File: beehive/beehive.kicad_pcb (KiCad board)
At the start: 2 copper layers, 23 parts, among them J1 M05PTH, Q1 MMBT4403, U1 ESP32-S3-WROOM-1U, U2 HX711, U3 ADXL362

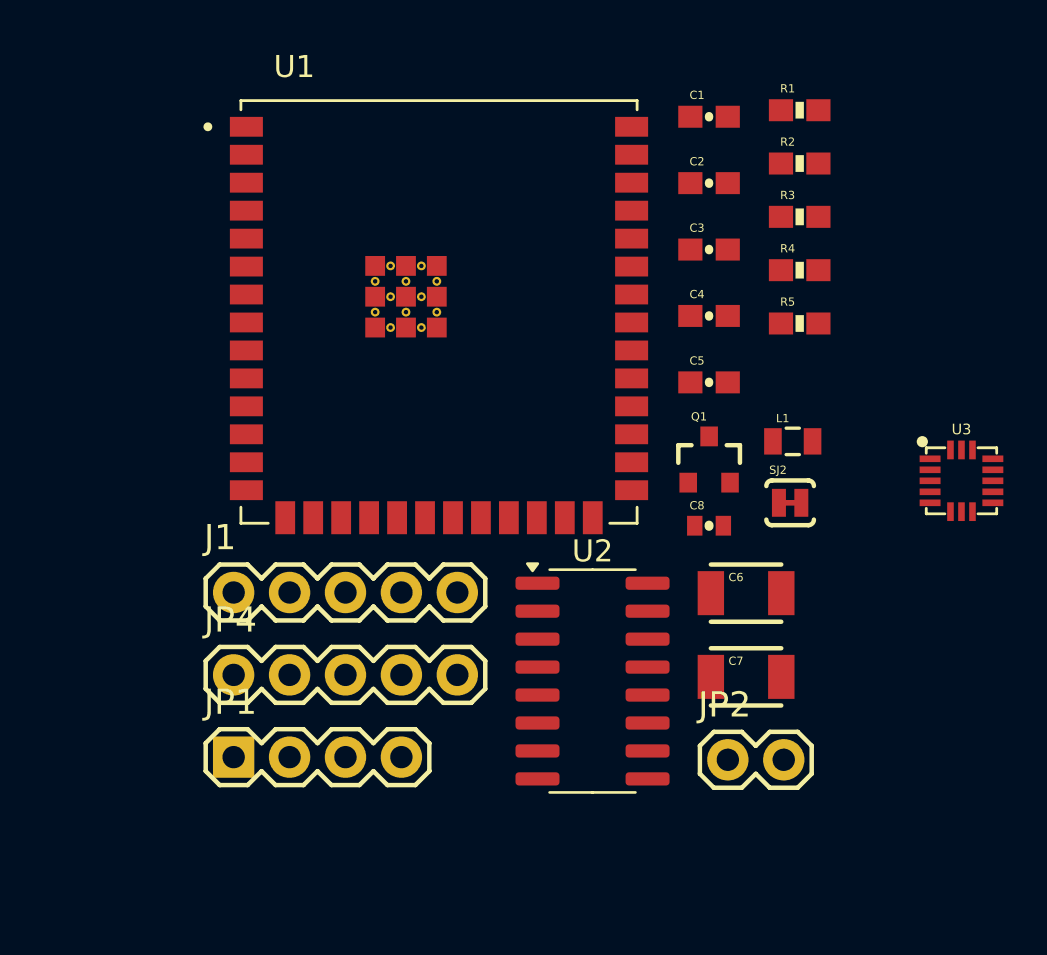
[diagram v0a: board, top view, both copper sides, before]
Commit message: added custom library submodule
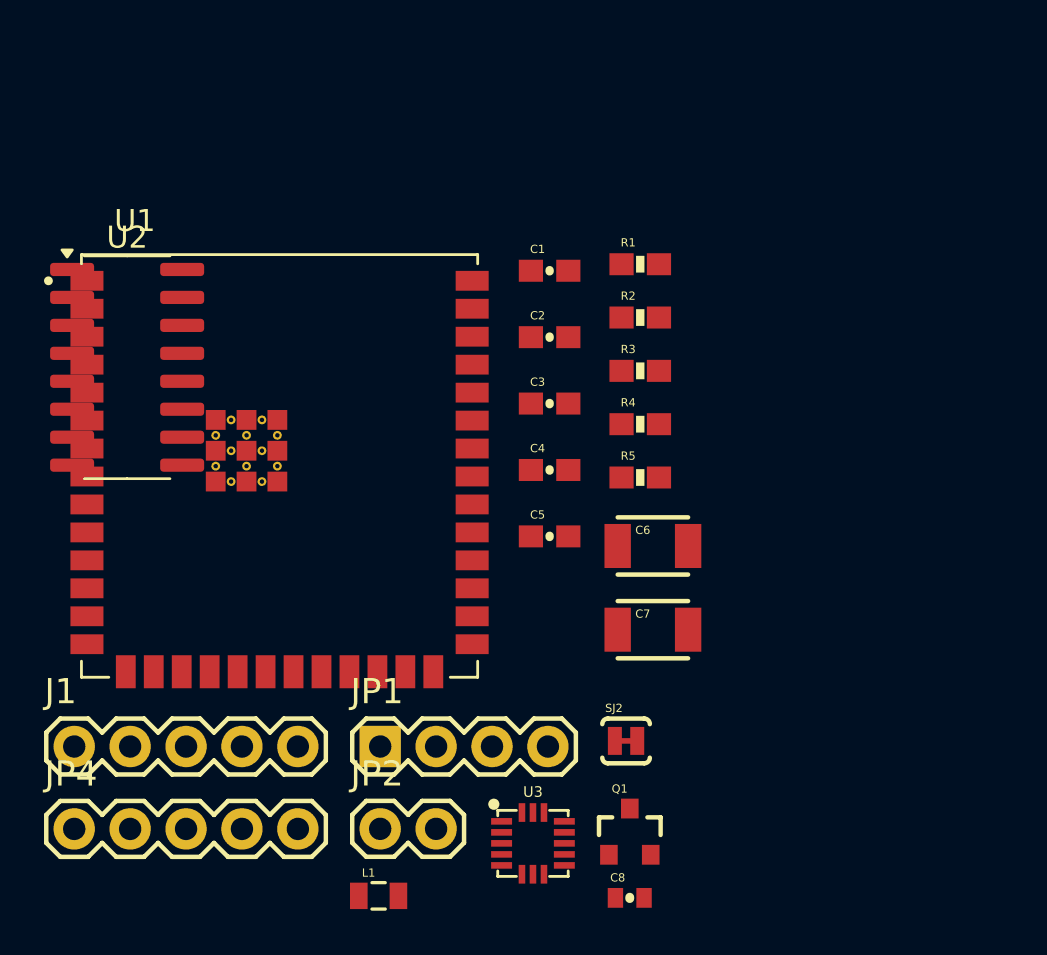
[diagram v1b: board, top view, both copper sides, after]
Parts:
- C1, C2, C3, C4, C5: footprint SparkFun_HX711_Load_Cell:0603-CAP -> Board_SparkFun_HX711_Load_Cell:0603-CAP
- C6, C7: footprint SparkFun_HX711_Load_Cell:1210 -> Board_SparkFun_HX711_Load_Cell:1210
- C8: footprint ADXL362 BOB v01:0402-CAP -> Board_ADXL362_BOB_v01:0402-CAP
- J1, JP4: footprint SparkFun_HX711_Load_Cell:1X05 -> Board_SparkFun_HX711_Load_Cell:1X05
- JP1: footprint ADXL362 BOB v01:1X04 -> Board_ADXL362_BOB_v01:1X04
- JP2: footprint SparkFun_HX711_Load_Cell:1X02 -> Board_SparkFun_HX711_Load_Cell:1X02
- L1: footprint SparkFun_HX711_Load_Cell:0805 -> Board_SparkFun_HX711_Load_Cell:0805
- Q1: footprint SparkFun_HX711_Load_Cell:SOT23-3 -> Board_SparkFun_HX711_Load_Cell:SOT23-3
- R1, R2, R3, R4, R5: footprint SparkFun_HX711_Load_Cell:0603-RES -> Board_SparkFun_HX711_Load_Cell:0603-RES
- SJ2: footprint SparkFun_HX711_Load_Cell:PAD-JUMPER-2-NC_BY_TRACE_YES_SILK -> Board_SparkFun_HX711_Load_Cell:PAD-JUMPER-2-NC_BY_TRACE_YES_SILK
- U1: footprint ESP32:XCVR_ESP32-S3-WROOM-1U -> ESP32-S3-WROOM-1:XCVR_ESP32-S3-WROOM-1U
- U3: footprint adxl362:LGA-16-3X2.5 -> ADXL362:LGA-16-3X2.5
- moved L1 27.9 mm to (103.6, 78.7)
- moved U3 25.5 mm to (110.6, 76.3)
- moved U2 25.5 mm to (92.2, 54.7)
- moved C8 17.3 mm to (115.0, 78.8)
- moved Q1 17.3 mm to (115.0, 75.8)
- moved JP2 16.1 mm to (103.7, 75.6)
- moved SJ2 13.1 mm to (114.8, 71.6)
- moved C1 10.1 mm to (111.4, 50.3)
- moved C3 10.1 mm to (111.4, 56.3)
- moved C5 10.1 mm to (111.4, 62.4)
- moved J1 10.1 mm to (89.8, 71.9)
- moved JP4 10.1 mm to (89.8, 75.6)
- moved R2 10.1 mm to (115.5, 52.4)
- moved R3 10.1 mm to (115.5, 54.8)
- moved R4 10.1 mm to (115.5, 57.3)
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
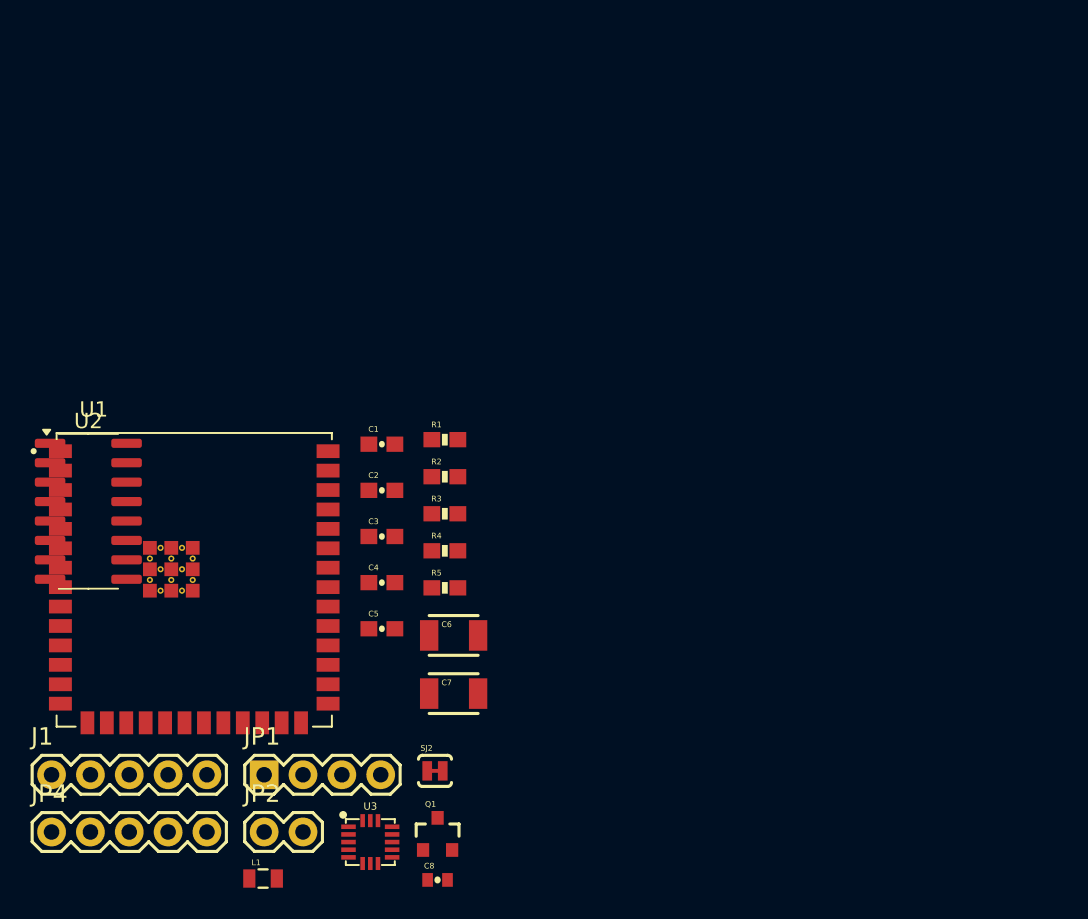
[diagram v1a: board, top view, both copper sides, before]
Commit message: TP5100 and ESP32 remaining
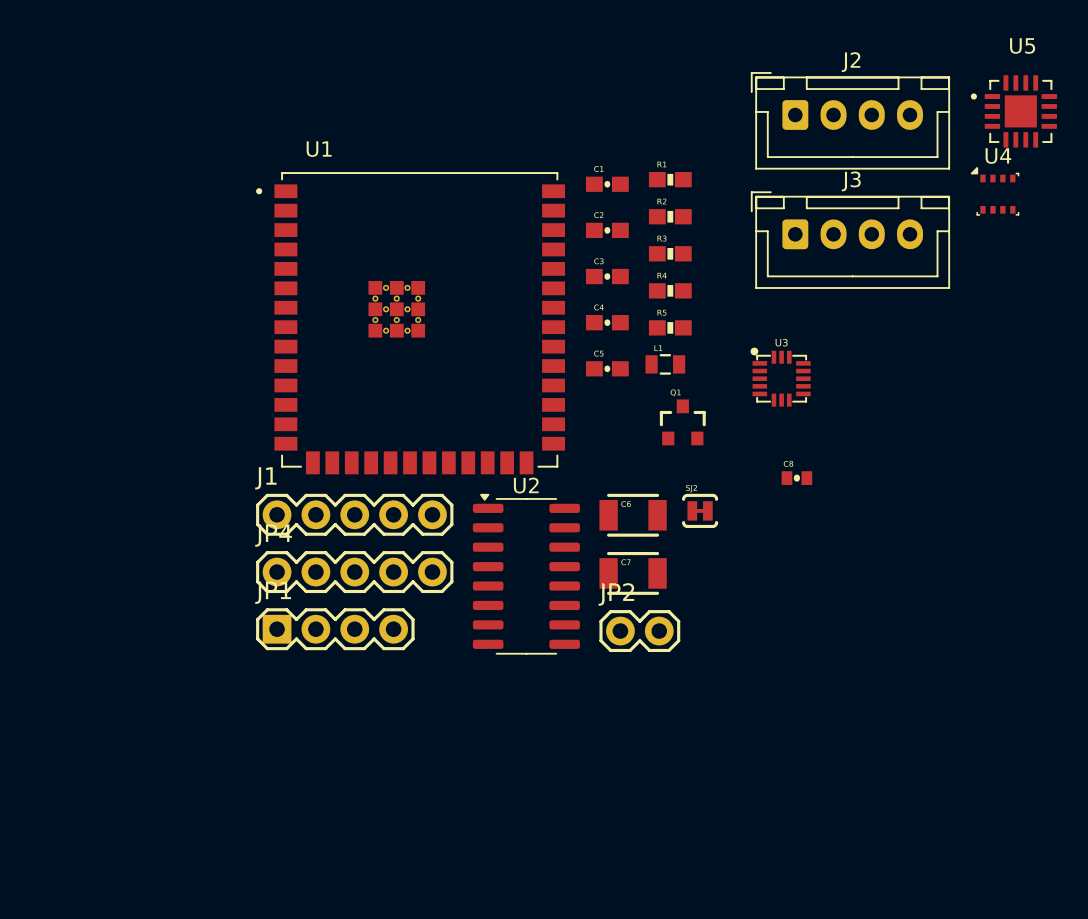
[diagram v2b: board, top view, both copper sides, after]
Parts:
- added J2: Conn_01x04_Pin, Connector_JST:JST_XH_B4B-XH-A_1x04_P2.50mm_Vertical, F.Cu at (138.4, 28.8)
- added J3: Conn_01x04_Pin, Connector_JST:JST_XH_B4B-XH-A_1x04_P2.50mm_Vertical, F.Cu at (138.4, 36.6)
- added U4: BME280, Package_LGA:Bosch_LGA-8_2.5x2.5mm_P0.65mm_ClockwisePinNumbering, F.Cu at (151.6, 33.9)
- added U5: TP5100, TP5100:QFN65P400X400X90-17N, F.Cu at (153.1, 28.5)
- moved L1 42.7 mm to (129.9, 45.1)
- moved U3 40.5 mm to (137.5, 46.0)
- moved C8 35.2 mm to (138.5, 52.5)
- moved Q1 31.3 mm to (131.0, 48.9)
- moved U2 29.0 mm to (120.8, 58.9)
- moved JP2 26.7 mm to (127.0, 62.5)
- moved SJ2 24.3 mm to (132.2, 54.6)
- moved J1 22.5 mm to (104.5, 54.9)
- moved C1 22.5 mm to (126.1, 33.3)
- moved C3 22.5 mm to (126.1, 39.3)
- moved C5 22.5 mm to (126.1, 45.4)
- moved C2 22.5 mm to (126.1, 36.3)
- moved C4 22.5 mm to (126.1, 42.3)
- moved JP4 22.5 mm to (104.5, 58.6)
- moved R2 22.5 mm to (130.2, 35.4)
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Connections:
- C4 pad 2: GND -> unconnected-(C4-Pad2)
- C5 pad 2: GND -> unconnected-(C5-Pad2)
- C6 pad 2: GND -> unconnected-(C6-Pad2)
- U3 pad P$1: unconnected-(U3-VDDIO-PadP$1) -> 3.3V
- U3 pad P$11: unconnected-(U3-INT1-PadP$11) -> Net-(J2-Pin_3)
- U3 pad P$12: Net-(U3-GND-PadP$12) -> GND
- U3 pad P$13: Net-(U3-GND-PadP$12) -> GND
- U3 pad P$14: unconnected-(U3-VS-PadP$14) -> 3.3V
- U3 pad P$16: Net-(U3-GND-PadP$12) -> GND
- U3 pad P$4: unconnected-(U3-SCLK-PadP$4) -> Net-(J3-Pin_4)
- U3 pad P$6: unconnected-(U3-MOSI-PadP$6) -> Net-(J3-Pin_3)
- U3 pad P$7: unconnected-(U3-MISO-PadP$7) -> Net-(J3-Pin_2)
- U3 pad P$8: unconnected-(U3-~{CS}-PadP$8) -> Net-(J3-Pin_1)
- U3 pad P$9: unconnected-(U3-INT2-PadP$9) -> Net-(J2-Pin_4)

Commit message: 123
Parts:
- added C10: 10uF/25V, Capacitor_SMD:C_0603_1608Metric_Pad1.08x0.95mm_HandSolder, F.Cu at (170.3, 85.8)
- added C9: 10uF/25V, Capacitor_SMD:C_0603_1608Metric_Pad1.08x0.95mm_HandSolder, F.Cu at (170.3, 83.3)
- added IC1: MP2307, MP2307:SO8-TH, F.Cu at (165.1, 86.3)
- added U6: MCP1700x-330xxTT, Package_TO_SOT_SMD:SOT-23, F.Cu at (170.6, 89.5)
- C8: value .1uF -> 0.1uF
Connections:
- net 3.3V renamed +3.3V
- C4 pad 2: unconnected-(C4-Pad2) -> GND
- C5 pad 2: unconnected-(C5-Pad2) -> GND
- C6 pad 2: unconnected-(C6-Pad2) -> GND

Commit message: last
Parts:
- added C20: 10uF, Capacitor_SMD:C_0603_1608Metric_Pad1.08x0.95mm_HandSolder, F.Cu at (1.68, 8.55)
- added C21: 10uF, Capacitor_SMD:C_0603_1608Metric_Pad1.08x0.95mm_HandSolder, F.Cu at (1.68, 11.1)
- added C23: 10uF, Capacitor_SMD:C_0603_1608Metric_Pad1.08x0.95mm_HandSolder, F.Cu at (1.68, 13.6)
- added C25: 10uF, Capacitor_SMD:C_0603_1608Metric_Pad1.08x0.95mm_HandSolder, F.Cu at (1.68, 16.1)
- added J4: Conn_01x07_Socket, Connector_JST:JST_XH_B7B-XH-A_1x07_P2.50mm_Vertical, F.Cu at (2.98, 2.88)
- added R12: 10k, Board_SparkFun_HX711_Load_Cell:0603-RES, F.Cu at (10.7, 8.51)
- added R13: 100, Board_SparkFun_HX711_Load_Cell:0603-RES, F.Cu at (10.7, 10.9)
- added R14: 5.1k, Resistor_SMD:R_0805_2012Metric_Pad1.20x1.40mm_HandSolder, F.Cu at (6.22, 8.78)
- added R15: 5.1k, Resistor_SMD:R_0805_2012Metric_Pad1.20x1.40mm_HandSolder, F.Cu at (6.22, 11.7)
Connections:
- net /SCK renamed SCK
- net Net-(U5-VIN-Pad1) renamed +12V
- U1 pad 1: Net-(U1-GND-Pad1) -> GND
- U1 pad 13: unconnected-(U1-IO19-Pad13) -> D-
- U1 pad 14: unconnected-(U1-IO20-Pad14) -> D+
- U1 pad 2: unconnected-(U1-3V3-Pad2) -> +3.3V
- U1 pad 27: unconnected-(U1-IO0-Pad27) -> BOOT
- U1 pad 3: unconnected-(U1-EN-Pad3) -> EN
- U1 pad 40: Net-(U1-GND-Pad1) -> GND
- U1 pad 41_1: Net-(U1-GND-Pad1) -> GND
- U1 pad 41_2: Net-(U1-GND-Pad1) -> GND
- U1 pad 41_3: Net-(U1-GND-Pad1) -> GND
- U1 pad 41_4: Net-(U1-GND-Pad1) -> GND
- U1 pad 41_5: Net-(U1-GND-Pad1) -> GND
- U1 pad 41_6: Net-(U1-GND-Pad1) -> GND
- U1 pad 41_7: Net-(U1-GND-Pad1) -> GND
- U1 pad 41_8: Net-(U1-GND-Pad1) -> GND
- U1 pad 41_9: Net-(U1-GND-Pad1) -> GND
- U5 pad 10: unconnected-(U5-VREG-Pad10) -> Net-(BT1--)
- U5 pad 11: unconnected-(U5-TS-Pad11) -> GND
- U5 pad 12: unconnected-(U5-RTRICK-Pad12) -> Net-(BT1--)
- U5 pad 13: unconnected-(U5-CS-Pad13) -> Net-(BT1--)
- U5 pad 14: unconnected-(U5-~{STDBY}-Pad14) -> Net-(D2-K)
- U5 pad 15: unconnected-(U5-~{CHRG}-Pad15) -> Net-(D1-K)
- U5 pad 17: unconnected-(U5-EXP-Pad17) -> GND
- U5 pad 7: unconnected-(U5-GND-Pad7) -> GND
- U5 pad 8: unconnected-(U5-VS-Pad8) -> Net-(U5-VS)
- U5 pad 9: unconnected-(U5-BAT-Pad9) -> Net-(BT1-+)
